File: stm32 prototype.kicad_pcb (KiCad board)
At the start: 4 copper layers, 86 x 64 mm, 98 parts, among them J1 Conn_01x04, J10 Conn_01x03, J12 Conn_01x07, J13 Conn_01x06, J14 Conn_01x30, J2 Conn_02x05_Odd_Even, J3 Conn_01x08, J4 Conn_01x06, J5 Conn_01x06, J6 Conn_01x06, J7 Conn_01x06, J8 Conn_ARM_JTAG_SWD_10, J9 Conn_01x03, Q1 Q_NMOS_GSD, Q2 Q_NMOS_GSD, Q3 Q_NMOS_GSD, Q4 Q_NMOS_GSD, Q5 Q_NMOS_GSD, Q6 Q_NMOS_GSD, Q7 Q_NMOS_GSD, Q8 Q_NMOS_GSD, SW1 SW_Push, SW2 SW_Push, U3 STM32F407VGTx, U7 TPS62203DBVR, Y1 Crystal_GND24, Y2 Crystal_GND24

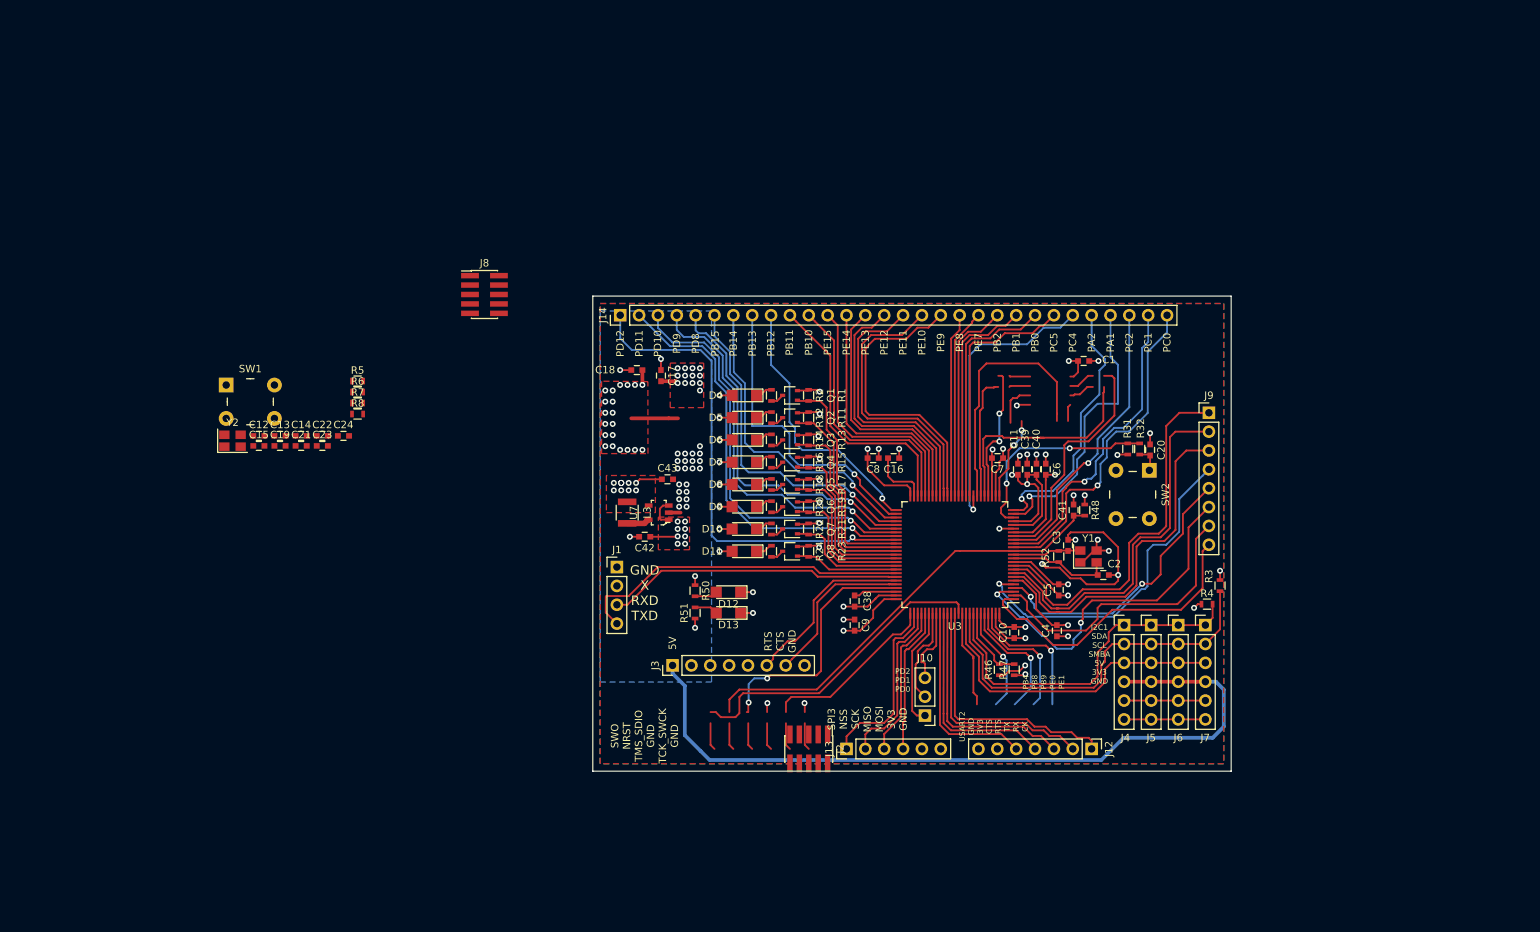
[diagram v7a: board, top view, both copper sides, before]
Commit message: Worked on layout for new MCU
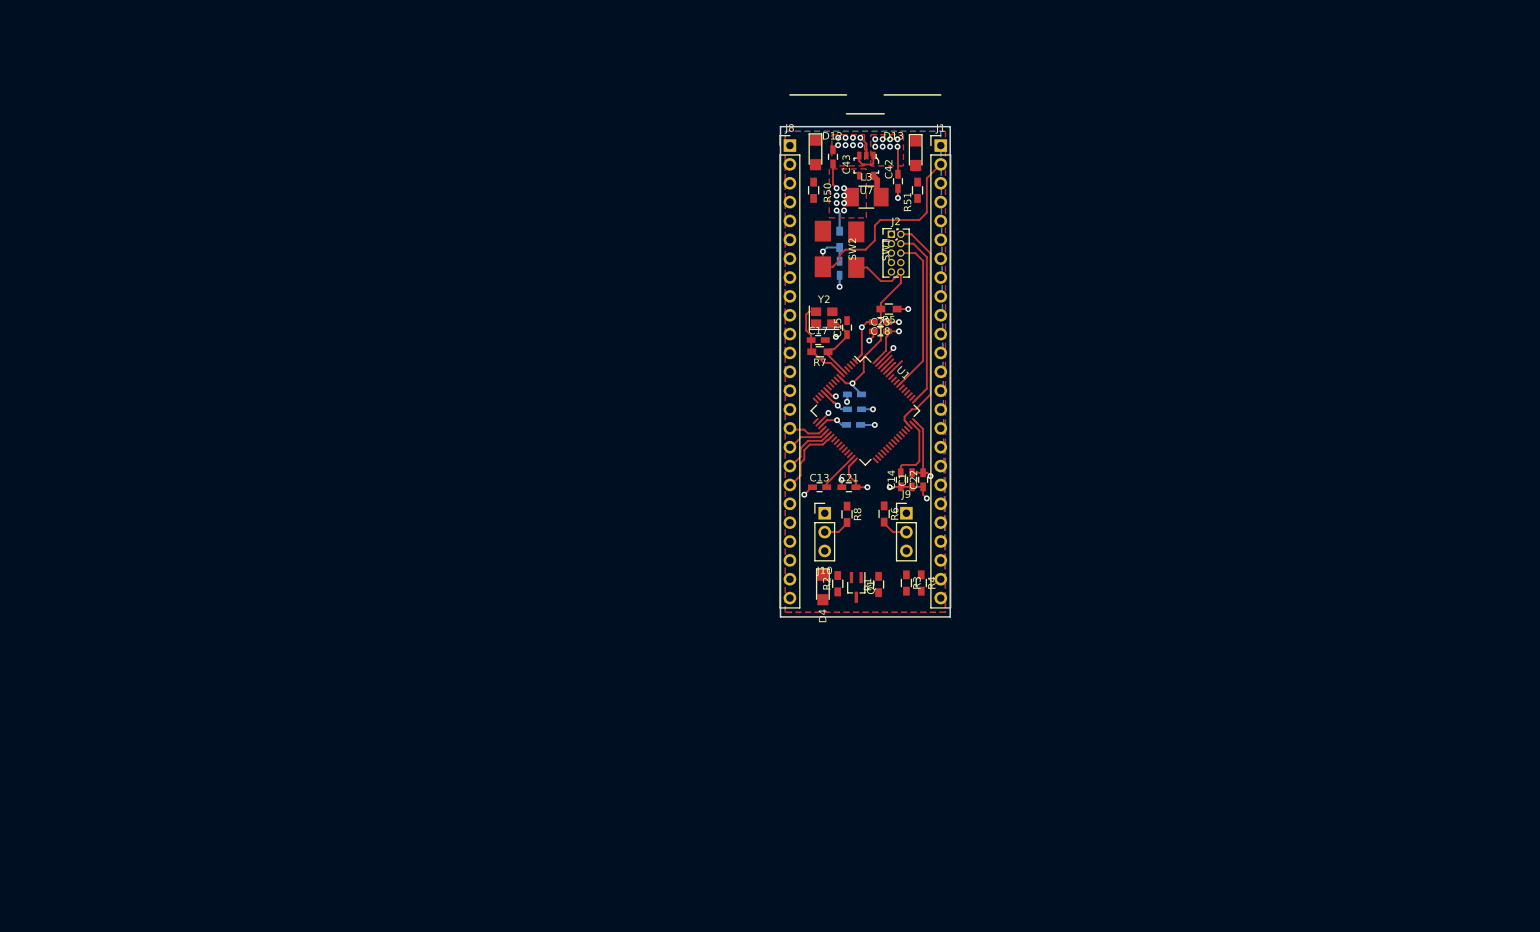
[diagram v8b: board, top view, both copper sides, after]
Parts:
- removed C10, C11, C39, C41, C5, C6, C7, C8, C9: .1uF, Capacitors_SMD:C_0603
- removed C16, C38: 2.2uF, Capacitors_SMD:C_0603
- removed C2, C3: 9pF, Capacitors_SMD:C_0603
- removed C4, C40: 1uF, Capacitors_SMD:C_0603
- removed D10, D11, D5, D6, D7, D8, D9: LED, LEDs:LED_1206
- removed J12: Conn_01x07, Pin_Headers:Pin_Header_Straight_1x07_Pitch2.54mm
- removed J13, J4, J5, J6, J7: Conn_01x06, Pin_Headers:Pin_Header_Straight_1x06_Pitch2.54mm
- removed J14: Conn_01x30, Pin_Headers:Pin_Header_Straight_1x30_Pitch2.54mm
- removed J3: Conn_01x08, Pin_Headers:Pin_Header_Straight_1x08_Pitch2.54mm
- removed Q2, Q3, Q4, Q5, Q6, Q7, Q8: Q_NMOS_GSD, TO_SOT_Packages_SMD:SOT-323_SC-70
- removed R11, R13, R15, R17, R19, R21, R23, R47: 10K, Resistors_SMD:R_0603
- removed R12, R14, R16, R18, R20, R22, R24: 330R, Resistors_SMD:R_0603
- removed R31: 10k, Resistors_SMD:R_0603
- removed R46: DNP, Resistors_SMD:R_0603
- removed R48: 100K, Resistors_SMD:R_0603
- removed R52: 1MR, Resistors_SMD:R_0603
- removed U3: STM32F407VGTx, Housings_QFP:LQFP-100_14x14mm_Pitch0.5mm
- removed Y1: Crystal_GND24, Crystals:Crystal_SMD_SeikoEpson_TSX3225-4pin_3.2x2.5mm
- added U1: STM32F405RGTx, Housings_QFP:LQFP-64_10x10mm_Pitch0.5mm, F.Cu at (172.7, 81.5)
- C1, C13, C14, C15, C17, C18, C21, C22, C23, C42, C43: footprint Capacitors_SMD:C_0603 -> Capacitors_SMD:C_0603_HandSoldering
- C12, C19, C20, C24: footprint Capacitors_SMD:C_0603 -> Capacitors_SMD:C_0603_HandSoldering; moved to B.Cu
- J1: value Conn_01x04 -> Conn_01x25; footprint Pin_Headers:Pin_Header_Straight_1x04_Pitch2.54mm -> Pin_Headers:Pin_Header_Straight_1x25_Pitch2.54mm
- J2: footprint Pin_Headers:Pin_Header_Straight_2x05_Pitch1.27mm_SMD -> Pin_Headers:Pin_Header_Straight_2x05_Pitch1.27mm
- J8: value Conn_ARM_JTAG_SWD_10 -> Conn_01x25; footprint Pin_Headers:Pin_Header_Straight_2x05_Pitch1.27mm_SMD -> Pin_Headers:Pin_Header_Straight_1x25_Pitch2.54mm
- J9: footprint Pin_Headers:Pin_Header_Straight_1x08_Pitch2.54mm -> Pin_Headers:Pin_Header_Straight_1x03_Pitch2.54mm
- L3: footprint Inductors_SMD:L_1210 -> Inductors_SMD:L_1210_HandSoldering
- Q1: footprint TO_SOT_Packages_SMD:SOT-323_SC-70 -> TO_SOT_Packages_SMD:SOT-323_SC-70_Handsoldering
- R1, R2, R3, R4, R5, R50, R51, R6, R7, R8: footprint Resistors_SMD:R_0603 -> Resistors_SMD:R_0603_HandSoldering
- R32: value 470R -> 10k; footprint Resistors_SMD:R_0603 -> Resistors_SMD:R_0603_HandSoldering; moved to B.Cu
- SW1, SW2: footprint switches_mdg:Switch_Tactile_6x6mm_Vertical_SMD_MJTP1230 -> switches_mdg:FSM2JMTR
- moved SW1 84.2 mm to (171.5, 59.8), turned to 90 degrees
- moved Y2 81.4 mm to (167.2, 68.9)
- moved C22 81.1 mm to (180.5, 90.8), turned to 90 degrees
- moved C14 81.0 mm to (177.5, 90.8), turned to 90 degrees
- moved C15 80.8 mm to (170.2, 70.2), turned to 90 degrees
- moved C12 80.4 mm to (171.2, 79.2)
- moved C19 77.3 mm to (171.1, 83.4), turned to 180 degrees
- moved C23 76.7 mm to (174.8, 70.8)
- moved C21 74.0 mm to (170.5, 91.8)
- moved C13 73.0 mm to (166.6, 91.8)
- moved R6 72.8 mm to (175.2, 95.3), turned to 270 degrees
- moved R5 72.2 mm to (175.9, 67.8), turned to 180 degrees
- moved J1 71.6 mm to (182.9, 45.7)
- moved J2 70.2 mm to (176.2, 57.7), turned to 0 degrees
- moved C24 68.9 mm to (171.2, 81.2), turned to 180 degrees
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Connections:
- C12 pad 2: Net-(C12-Pad2) -> NRST
- C13 pad 2: (no net) -> Net-(C13-Pad2)
- C14 pad 2: (no net) -> Net-(C14-Pad2)
- C20 pad 2: Net-(C20-Pad2) -> PA0
- J1 pad 1: GND -> +5V
- J1 pad 2: (no net) -> PA0
- J1 pad 3: FTDI_ST_TXD -> PA1
- J1 pad 4: FTDI_ST_RXD -> PA2
- J8 pad 10: NRST -> PC7
- J8 pad 2: TMS_SWDIO -> PD2
- J8 pad 3: GND -> PC0
- J8 pad 4: TCK_SWCLK -> PC1
- J8 pad 5: GND -> PC2
- J8 pad 6: SWO -> PC3
- J8 pad 7: (no net) -> PC4
- J8 pad 8: (no net) -> PC5
- J8 pad 9: GND -> PC6
- Q1 pad 1: STATUS_BIT0 -> PC15_STATUS
- R1 pad 1: STATUS_BIT0 -> PC15_STATUS
- R3 pad 2: I2C1_SCL -> PB6_I2C1_SCL
- R32 pad 1: Net-(R31-Pad2) -> +3V3
- R32 pad 2: Net-(C20-Pad2) -> PA0
- R4 pad 2: I2C1_SDA -> PB7_I2C1_SDA
- R5 pad 2: Net-(C12-Pad2) -> NRST
- R6 pad 1: (no net) -> Net-(R6-Pad1)
- R8 pad 1: (no net) -> Net-(R8-Pad1)
- SW1 pad 1: Net-(C12-Pad2) -> NRST
- SW1 pad 2: (no net) -> GND
- SW2 pad 1: Net-(C20-Pad2) -> PA0
- SW2 pad 2: (no net) -> GND
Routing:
- net (no net): track 435.2 -> 0.00 mm, vias 13 -> 0
- net GND: track 199.1 -> 28.8 mm, vias 58 -> 23
- net +3V3: track 194.3 -> 45.3 mm, vias 55 -> 15
- net +5V: track 113.7 -> 7.68 mm, vias 21 -> 8
- net PD12: track 65.7 -> 0.00 mm, vias 1 -> 0
- net PD11: track 57.2 -> 0.00 mm, vias 1 -> 0
- net PD10: track 55.5 -> 0.00 mm, vias 1 -> 0
- net I2C1_SCL: track 52.5 -> 0.00 mm
- net PD9: track 51.7 -> 0.00 mm, vias 1 -> 0
- net PD8: track 48.8 -> 0.00 mm, vias 1 -> 0
- net I2C1_SDA: track 48.7 -> 0.00 mm
- net Net-(J9-Pad2): track 49.4 -> 3.64 mm
- net PB15: track 45.7 -> 0.00 mm, vias 1 -> 0
- net FTDI_ST_RXD: track 45.5 -> 0.00 mm
- net PC0: track 44.8 -> 0.00 mm, vias 1 -> 0
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- removed copper zone on B.Cu, net +5V
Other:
- board size 86 x 64 mm -> 22.9 x 66 mm
- board text removed: "5V"
- board text removed: "GND X RXD TXD"
- board text removed: "I2C1 SDA SCL SMBA 5V 3V3 GND"
- board text removed: "PA1"
- board text removed: "PA2"
- board text removed: "PB0"
- board text removed: "PB1"
- board text removed: "PB10"
- board text removed: "PB11"
- board text removed: "PB12"
- board text removed: "PB13"
- board text removed: "PB14"
- board text removed: "PB15"
- board text removed: "PB2"
- board text removed: "PB4 PB8 PB9 PE0 PE1"
- board text removed: "PC0"
- board text removed: "PC1"
- board text removed: "PC2"
- board text removed: "PC4"
- board text removed: "PC5"
- board text removed: "PD10"
- board text removed: "PD11"
- board text removed: "PD12"
- board text removed: "PD2 PD1 PD0"
- board text removed: "PD8"
- board text removed: "PD9"
- board text removed: "PE10"
- board text removed: "PE11"
- board text removed: "PE12"
- board text removed: "PE13"
- board text removed: "PE14"
- board text removed: "PE15"
- board text removed: "PE7"
- board text removed: "PE8"
- board text removed: "PE9"
- board text removed: "RTS CTS GND"
- board text removed: "SPI3 NSS SCK MISO MOSI 3V3 GND"
- board text removed: "SWO NRST TMS_SDIO GND TCK_SWCK GND"
- board text removed: "USART2 GND 3V3 CTS RTS TX RX CK"
